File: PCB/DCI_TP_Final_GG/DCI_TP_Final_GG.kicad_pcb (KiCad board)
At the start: 2 copper layers, 69 parts, among them J201 DRIVER A OUT, J301 DRIVER B OUT, J401 IN - Driver A, J402 IN - Driver B, J403 Vin, J404 Vout, U201 A3967, U301 A3967, U401 LM317

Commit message: Avance en el routeo
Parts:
- moved C405 13.3 mm to (114.0, 98.4), turned to 270 degrees
- moved C403 7.00 mm to (128.0, 92.1)
- moved JP401 2.00 mm to (133.0, 96.9)
- moved R409 2.00 mm to (127.9, 98.0)
- moved R410 2.00 mm to (131.0, 96.9)
- moved R411 2.00 mm to (127.9, 96.0)
- moved U401 1.50 mm to (121.7, 96.0)
- moved TP403 0.71 mm to (115.5, 95.5)
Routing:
- net VCC: track 0.00 -> 51.5 mm
- net GND: track 0.00 -> 47.0 mm, vias 0 -> 2
- net /Driver B/DB-O2A: track 0.00 -> 28.8 mm, vias 0 -> 1
- net /Driver B/ENA-B: track 0.00 -> 25.8 mm, vias 0 -> 1
- net /Driver B/DB-O2B: track 0.00 -> 25.2 mm, vias 0 -> 1
- net /Driver B/RST-B: track 0.00 -> 24.9 mm, vias 0 -> 1
- net VDD: track 0.00 -> 24.6 mm
- net /Driver B/MS2-B: track 0.00 -> 22.3 mm
- net /Driver B/DB-O1B: track 0.00 -> 15.7 mm
- net /Driver B/DB-O1A: track 0.00 -> 15.1 mm
- net /Driver B/MS1-B: track 0.00 -> 13.1 mm
- net /Driver B/SLEEP-B: track 0.00 -> 9.38 mm
- net Net-(J402-Pad7): track 0.00 -> 8.53 mm
- net Net-(J402-Pad6): track 0.00 -> 6.18 mm
- net /Driver B/PFD-B: track 0.00 -> 6.16 mm
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- added copper zone on B.Cu, net GND
- added copper zone on F.Cu, net VDD
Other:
- net class Default: clearance 0.2 -> 0.3
- rule trace_clearance: 0.2 -> 0.3

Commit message: avance en pcb
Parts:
- moved R207 79.5 mm to (115.1, 90.0), turned to 180 degrees
- moved R202 77.4 mm to (114.5, 87.1)
- moved R401 42.0 mm to (97.0, 69.1)
- moved R403 42.0 mm to (86.2, 78.4)
- moved R405 42.0 mm to (91.6, 75.0)
- moved R406 42.0 mm to (101.4, 67.4)
- moved C405 31.4 mm to (141.0, 82.4)
- moved R412 5.62 mm to (116.0, 97.6)
- moved TP201 5.10 mm to (116.0, 83.0)
- moved J404 4.12 mm to (111.0, 93.0)
- moved TP403 2.55 mm to (115.0, 93.0)
- moved D401 2.07 mm to (110.5, 100.0), turned to 0 degrees
- moved RV201 2.00 mm to (120.0, 87.0)
- moved TP301 1.41 mm to (116.0, 101.0)
- moved R307 1.00 mm to (116.0, 106.0), turned to 270 degrees
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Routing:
- net VCC: track 51.5 -> 109.8 mm
- net /Driver B/PFD-B: track 6.16 -> 37.0 mm, vias 0 -> 2
- net /Driver B/ENA-B: track 25.8 -> 32.4 mm
- net /Driver B/SLEEP-B: track 9.38 -> 15.7 mm
- net Net-(C301-Pad1): track 0.00 -> 5.62 mm
- net /Driver B/RST-B: track 24.9 -> 29.9 mm, vias 1 -> 2
- net VDD: track 24.6 -> 28.1 mm
- net Net-(R307-Pad1): track 0.00 -> 3.38 mm
- net GND: track 47.0 -> 49.5 mm, vias 2 -> 7
- net Net-(RV301-Pad2): track 0.00 -> 2.00 mm
- net (no net): vias 0 -> 1
- added copper zone on F.Cu, net GND
- added copper zone on F.Cu, net VCC
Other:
- board outline added: 41.2 x 67.8 mm

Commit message: Avance en routeo
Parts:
- J403: footprint TerminalBlock:TerminalBlock_Altech_AK300-2_P5.00mm -> TerminalBlock_Phoenix:TerminalBlock_Phoenix_MKDS-1,5-2_1x02_P5.00mm_Horizontal
- moved R405 41.0 mm to (132.5, 78.4), turned to 270 degrees
- moved R403 39.9 mm to (126.0, 81.4), turned to 90 degrees
- moved R401 37.6 mm to (132.5, 81.6), turned to 270 degrees
- moved R406 30.1 mm to (128.0, 81.6), turned to 270 degrees
- moved C202 24.8 mm to (119.5, 62.5), turned to 180 degrees
- moved R212 23.6 mm to (119.6, 59.5), turned to 180 degrees
- moved R206 22.7 mm to (115.5, 64.1), turned to 90 degrees
- moved C405 21.8 mm to (133.5, 62.0), turned to 90 degrees
- moved R208 20.2 mm to (131.0, 62.0), turned to 90 degrees
- moved R209 19.2 mm to (126.9, 62.0), turned to 0 degrees
- moved R205 15.9 mm to (118.0, 66.1), turned to 90 degrees
- moved R203 10.8 mm to (122.5, 78.6), turned to 270 degrees
- moved J403 8.06 mm to (143.0, 98.0)
- moved J201 7.57 mm to (142.5, 69.0)
- moved C201 6.85 mm to (120.5, 78.6)
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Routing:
- net VCC: track 109.8 -> 153.0 mm, vias 0 -> 3
- net GND: track 49.5 -> 70.1 mm
- net VDD: track 28.1 -> 41.7 mm
- net Net-(D401-Pad2): track 0.00 -> 4.44 mm
- net /Driver B/RST-B: track 29.9 -> 25.6 mm
- net Net-(JP401-Pad1): track 0.00 -> 4.18 mm
- net Net-(R207-Pad1): track 0.00 -> 3.61 mm
- net Net-(RV301-Pad2): track 2.00 -> 4.00 mm
- net Net-(R307-Pad1): track 3.38 -> 4.38 mm
- net /Driver B/PFD-B: track 37.0 -> 37.7 mm
- net /Driver B/DB-O2B: track 25.2 -> 25.8 mm

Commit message: Avance en routeo
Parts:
- moved C405 19.0 mm to (133.5, 81.0), turned to 0 degrees
- moved R204 17.5 mm to (133.4, 69.2), turned to 0 degrees
- moved R401 17.3 mm to (115.2, 80.8), turned to 90 degrees
- moved R208 16.9 mm to (133.5, 78.8), turned to 0 degrees
- moved R212 16.9 mm to (135.0, 66.4), turned to 90 degrees
- moved R206 16.0 mm to (131.4, 63.0), turned to 0 degrees
- moved R405 15.2 mm to (117.5, 80.8)
- moved R203 14.1 mm to (122.1, 64.5), turned to 180 degrees
- moved R209 14.1 mm to (133.5, 74.4), turned to 270 degrees
- moved C202 14.1 mm to (133.0, 66.4), turned to 90 degrees
- moved J201 13.5 mm to (143.0, 82.5), turned to 90 degrees
- moved C201 12.7 mm to (115.5, 66.9), turned to 90 degrees
- moved R211 11.7 mm to (117.5, 66.9), turned to 90 degrees
- moved R403 11.5 mm to (115.2, 77.2), turned to 270 degrees
- moved R205 11.5 mm to (129.4, 65.5), turned to 0 degrees
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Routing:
- net VDD: track 41.7 -> 75.3 mm
- net /Driver A/DA-O2A: track 0.00 -> 25.0 mm, vias 0 -> 1
- net /Driver A/DA-O2B: track 0.00 -> 23.5 mm, vias 0 -> 1
- net /Driver A/DA-O1B: track 0.00 -> 16.8 mm
- net /Driver A/DA-O1A: track 0.00 -> 16.2 mm
- net GND: track 70.1 -> 82.4 mm, vias 7 -> 9

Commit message: avance en ruteo de PCB
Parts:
- moved R202 16.0 mm to (130.0, 83.0), turned to 0 degrees
- moved R206 15.5 mm to (116.0, 62.0), turned to 180 degrees
- moved R204 10.2 mm to (127.5, 60.9), turned to 90 degrees
- moved R203 4.62 mm to (125.0, 60.9), turned to 90 degrees
- moved R205 4.60 mm to (130.0, 60.9), turned to 270 degrees
- moved R211 4.00 mm to (115.0, 70.1), turned to 270 degrees
- moved C201 3.71 mm to (117.5, 70.1), turned to 270 degrees
- moved C402 2.50 mm to (132.5, 90.0), turned to 270 degrees
- moved TP201 1.80 mm to (116.5, 85.5)
- moved C405 1.21 mm to (134.2, 82.0)
- moved RV201 1.03 mm to (120.8, 88.0)
- moved R208 0.69 mm to (134.2, 78.8)
- moved C403 0.56 mm to (128.2, 91.6)
- moved JP401 0.56 mm to (133.2, 96.4)
- moved R409 0.56 mm to (128.2, 97.5)
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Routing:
- net VCC: track 153.0 -> 233.0 mm, vias 3 -> 5
- net /Driver A/MS2-A: track 0.00 -> 36.1 mm, vias 0 -> 2
- net /Driver A/PFD-A: track 0.00 -> 33.1 mm, vias 0 -> 2
- net /Driver A/RST-A: track 0.00 -> 29.4 mm
- net /Driver A/SLEEP-A: track 0.00 -> 26.6 mm, vias 0 -> 2
- net GND: track 82.4 -> 101.3 mm, vias 9 -> 10
- net /Driver A/MS1-A: track 0.00 -> 13.8 mm
- net Net-(J401-Pad7): track 0.00 -> 8.79 mm
- net Net-(J401-Pad6): track 0.00 -> 7.73 mm
- net Net-(C201-Pad1): track 0.00 -> 6.56 mm
- net Net-(C202-Pad1): track 0.00 -> 5.23 mm
- net Net-(R210-Pad2): track 0.00 -> 4.15 mm
- net Net-(R209-Pad2): track 0.00 -> 3.92 mm
- net /Driver A/STEP-A: track 0.00 -> 3.46 mm
- net /Driver A/DIR-A: track 0.00 -> 3.39 mm
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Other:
- board size 41.2 x 67.8 mm -> 41.5 x 72.8 mm

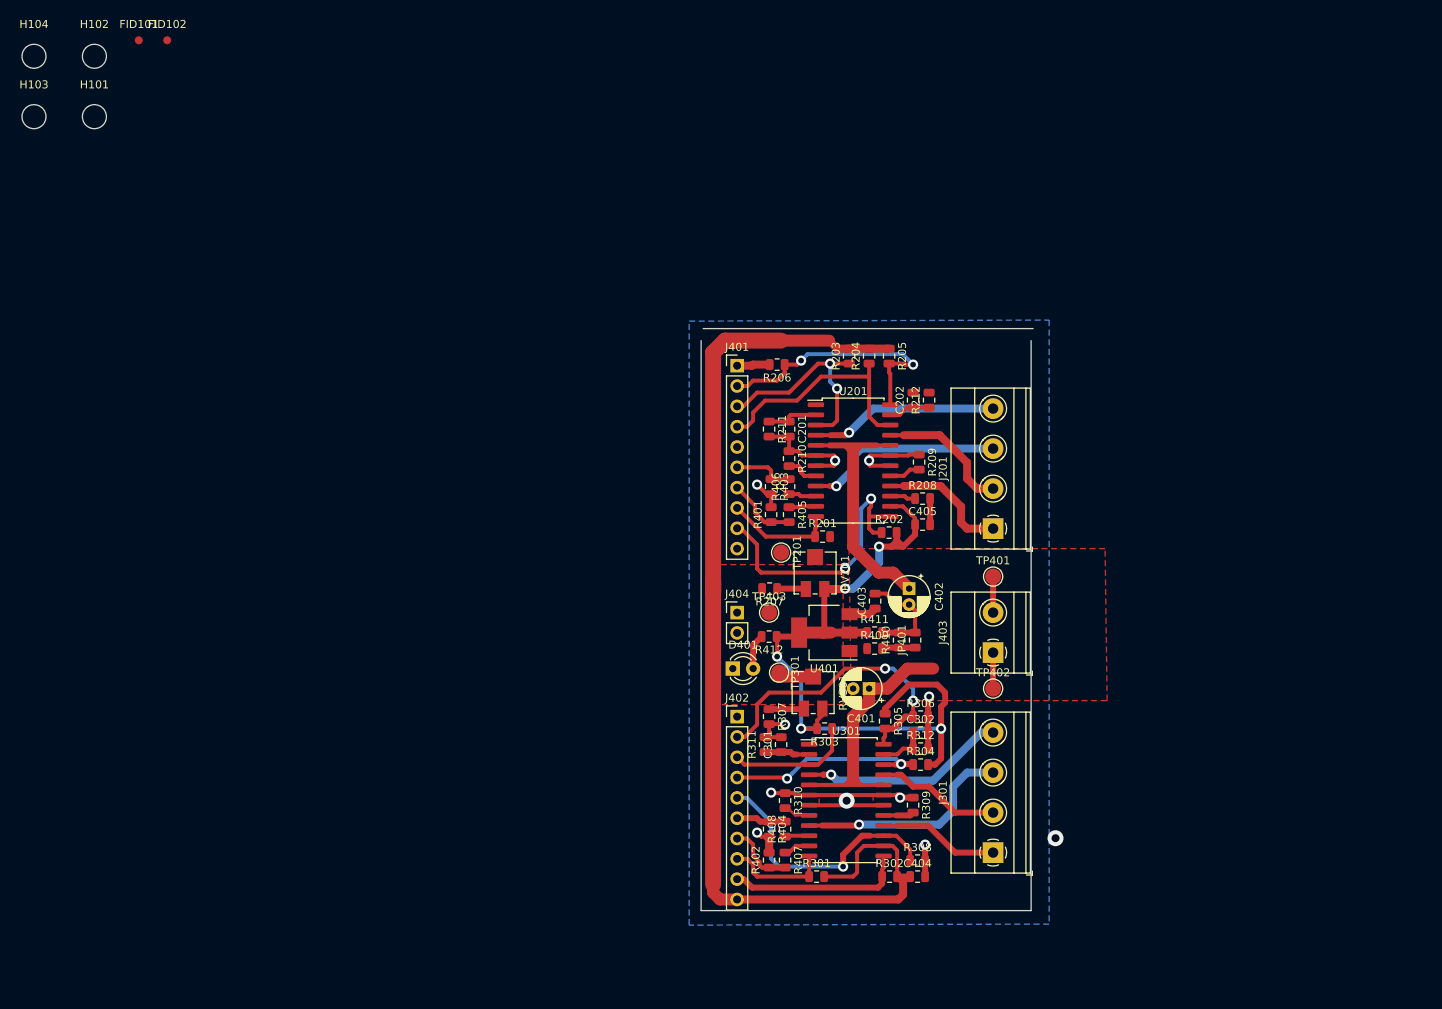
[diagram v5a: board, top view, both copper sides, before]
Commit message: Avance en routeo de PCB
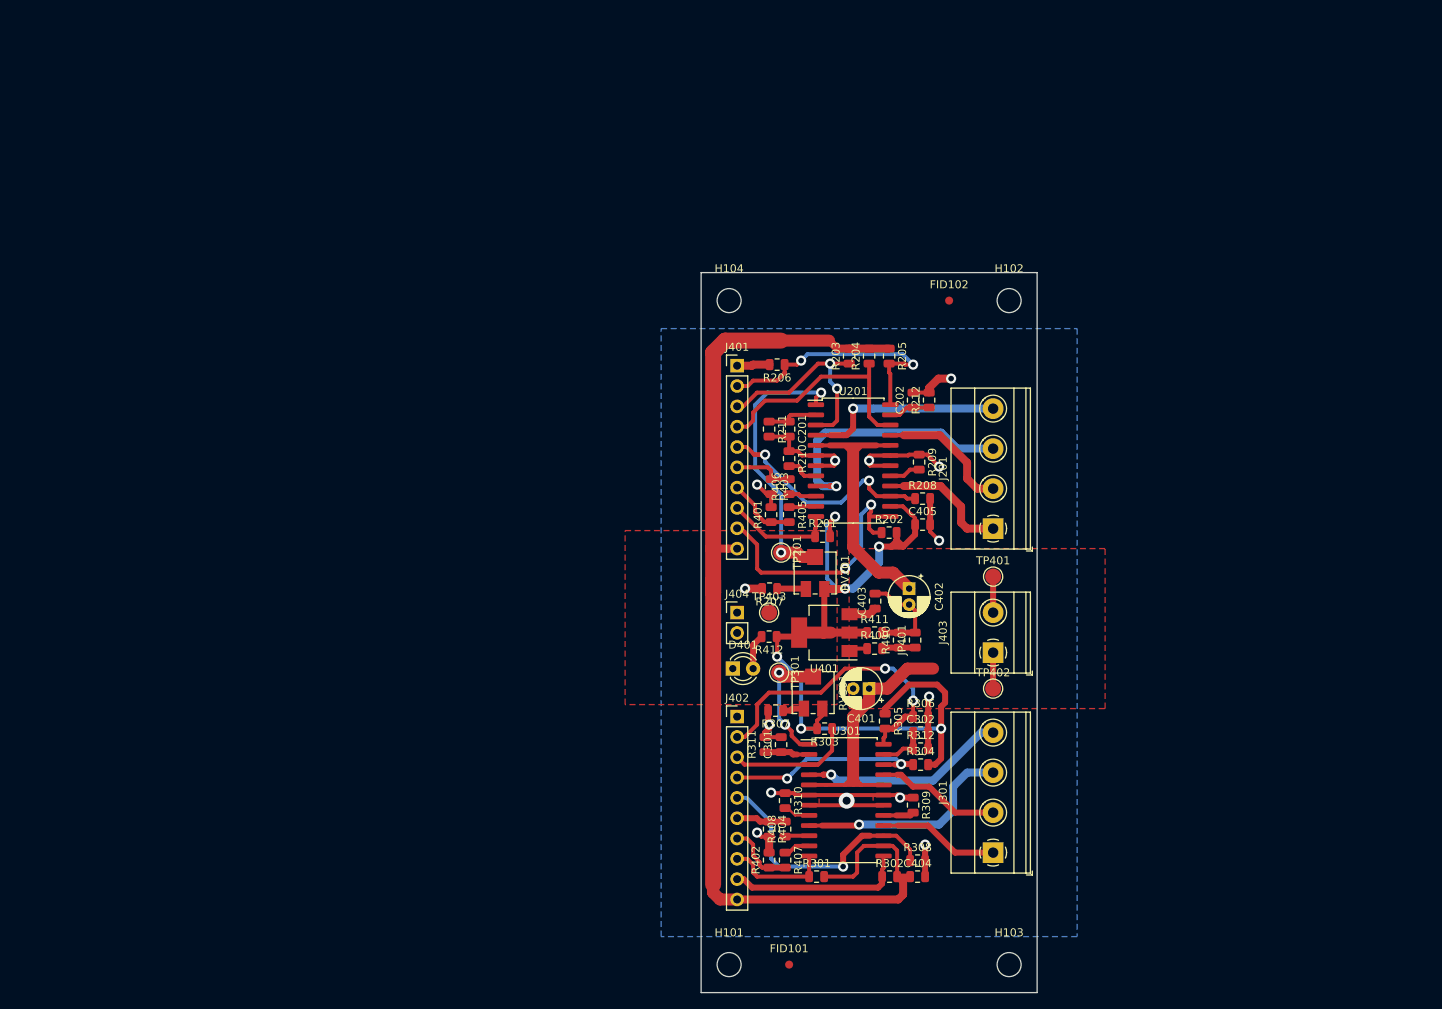
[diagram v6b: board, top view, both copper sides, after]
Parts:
- moved H103 161.5 mm to (145.0, 137.0)
- moved FID101 141.3 mm to (117.5, 137.0)
- moved H101 132.4 mm to (110.0, 137.0)
- moved H102 118.3 mm to (145.0, 54.0)
- moved FID102 103.0 mm to (137.5, 54.0)
- moved H104 92.1 mm to (110.0, 54.0)
- moved R307 1.11 mm to (115.8, 105.2), turned to 180 degrees
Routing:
- net Net-(RV201-Pad2): track 0.00 -> 35.0 mm, vias 0 -> 2
- net /Driver A/ENA-A: track 3.23 -> 30.2 mm, vias 0 -> 2
- net VCC: track 233.0 -> 249.7 mm, vias 5 -> 6
- net GND: track 101.3 -> 114.5 mm, vias 10 -> 14
- net Net-(RV301-Pad2): track 4.00 -> 15.6 mm, vias 0 -> 2
- net /Driver A/DA-O2A: track 25.0 -> 33.5 mm
- net Net-(R409-Pad1): track 0.00 -> 2.32 mm
- net Net-(R307-Pad1): track 4.38 -> 2.82 mm
- net /Driver A/MS2-A: track 36.1 -> 34.6 mm
- net /Driver A/DA-O2B: track 23.5 -> 25.0 mm
- net (no net): vias 1 -> 0
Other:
- board size 41.5 x 72.8 mm -> 42 x 90 mm

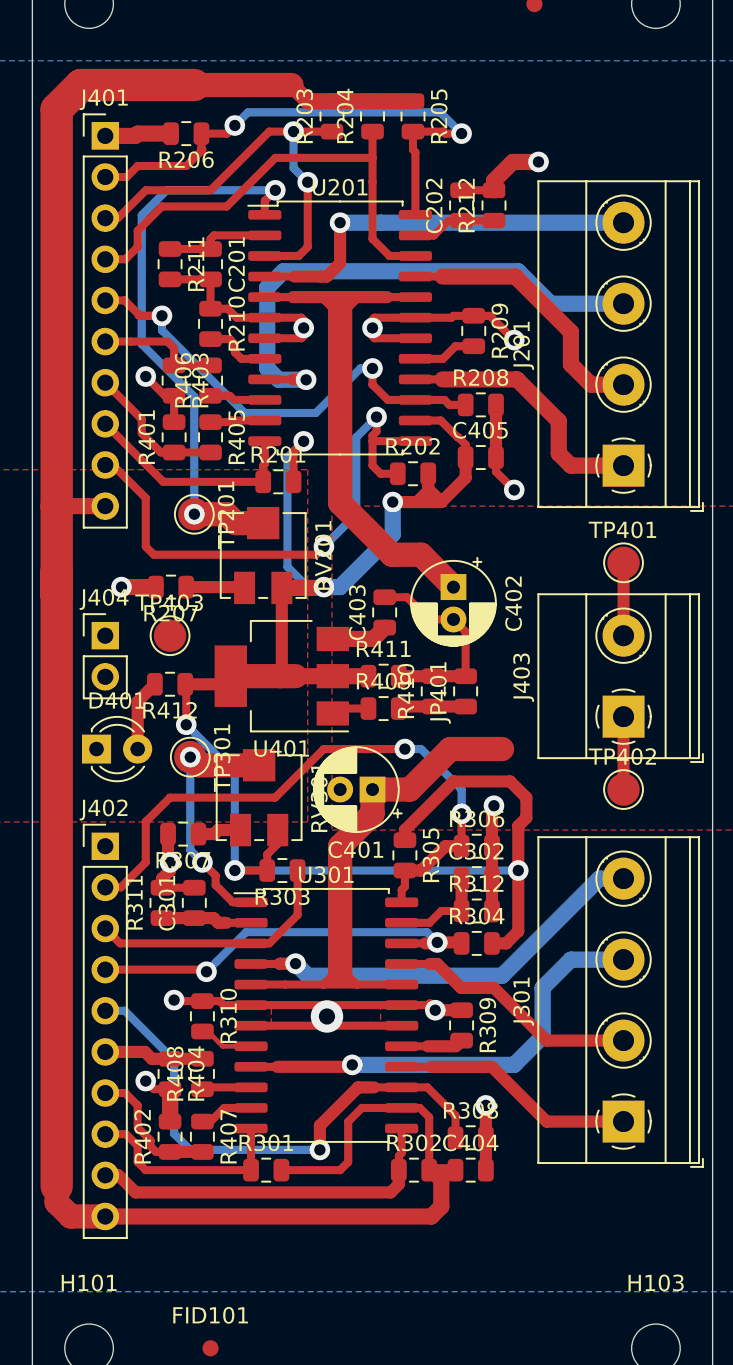
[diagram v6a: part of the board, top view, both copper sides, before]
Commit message: Avance en routeo de PCB
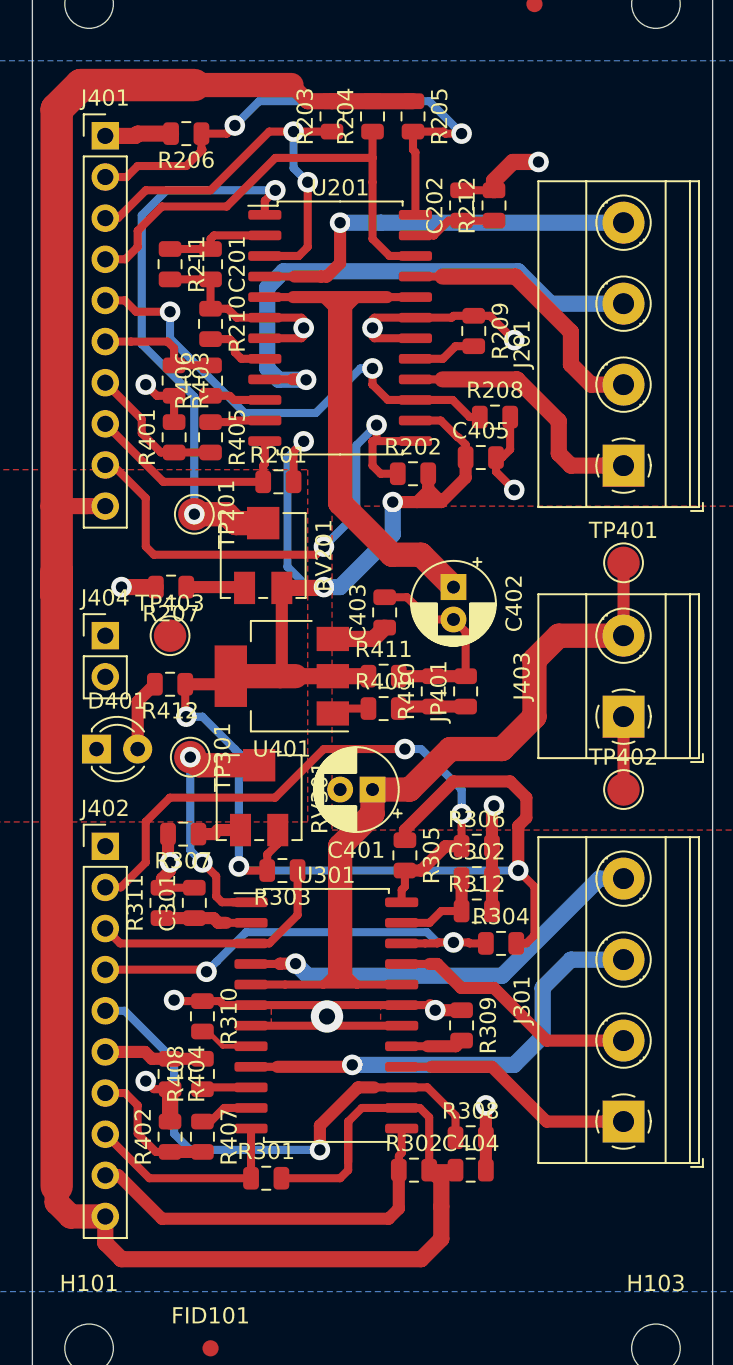
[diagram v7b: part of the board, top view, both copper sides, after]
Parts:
- moved R304 1.50 mm to (135.4, 112.0)
- moved R208 1.15 mm to (135.1, 79.5)
- moved R301 0.50 mm to (120.9, 126.5)
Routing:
- net VDD: track 77.6 -> 90.0 mm
- net VCC: track 249.7 -> 257.4 mm
- net /Driver B/RST-B: track 25.6 -> 28.1 mm
- net /Driver B/MS2-B: track 22.3 -> 24.5 mm
- net Net-(RV301-Pad2): track 15.6 -> 17.1 mm
- net /Driver A/MS2-A: track 34.6 -> 33.7 mm
- net /Driver A/PFD-A: track 33.1 -> 33.7 mm

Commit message: Avance en Routeo
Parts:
- moved R412 1.60 mm to (116.5, 96.6), turned to 270 degrees
- moved R310 1.00 mm to (116.0, 116.5)
- moved C302 0.94 mm to (133.0, 108.0)
- moved R312 0.94 mm to (133.0, 110.0)
- moved R207 0.80 mm to (114.4, 89.5)
- moved R307 0.75 mm to (115.8, 104.5)
- moved R210 0.25 mm to (117.2, 73.8)
- moved R405 0.25 mm to (117.2, 80.8)
- moved R406 0.25 mm to (117.2, 77.2)
- moved U301 0.06 mm to (124.7, 116.5)
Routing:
- net VCC: track 257.4 -> 268.3 mm
- net GND: track 114.7 -> 111.8 mm
- net /Driver B/DB-O2B: track 25.8 -> 27.8 mm
- net Net-(R310-Pad2): track 3.04 -> 4.38 mm
- net Net-(C302-Pad1): track 6.00 -> 4.75 mm
- net Net-(D401-Pad2): track 4.44 -> 5.41 mm
- net Net-(R207-Pad1): track 3.62 -> 4.45 mm
- net /Driver B/PFD-B: track 37.7 -> 38.3 mm
